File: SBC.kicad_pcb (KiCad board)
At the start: 4 copper layers, 0.6 x 0.9 mm, 128 parts, among them J1 MSD-1-A, J2 RJ45_Amphenol_RJMG1BD3B8K1ANR, J3 DX07S016JA1R1500, U1 MIC5501-3.0YM5, U10 USBLC6-2SC6, U11 USBLC6-2SC6, U12 USBLC6-2SC6, U2 TLV62569DBV, U3 TLV62569DBV, U4 TLV62569DBV, U5 Allwinner_V3s, U6 USBLC6-2SC6, U7 USBLC6-2SC6, U8 USBLC6-2SC6, U9 USBLC6-2SC6, Y1 Crystal

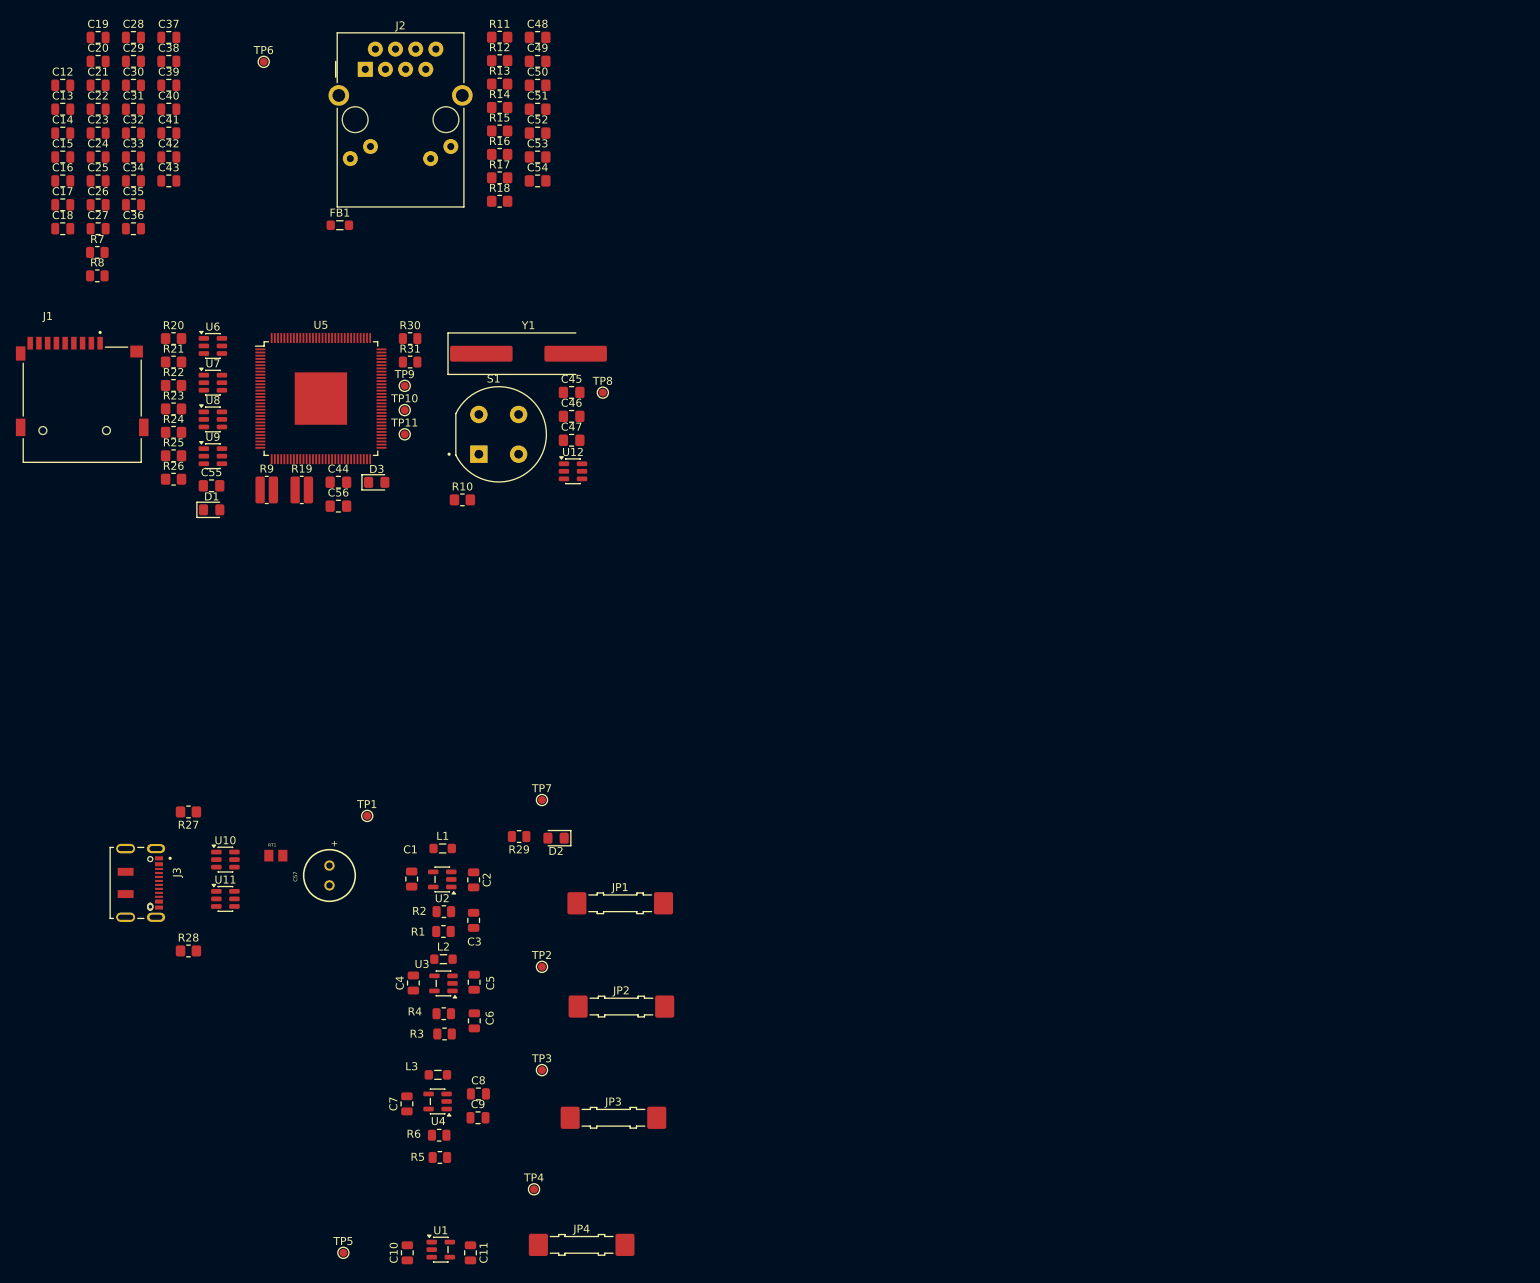
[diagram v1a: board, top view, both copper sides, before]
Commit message: arranged positions of all the components
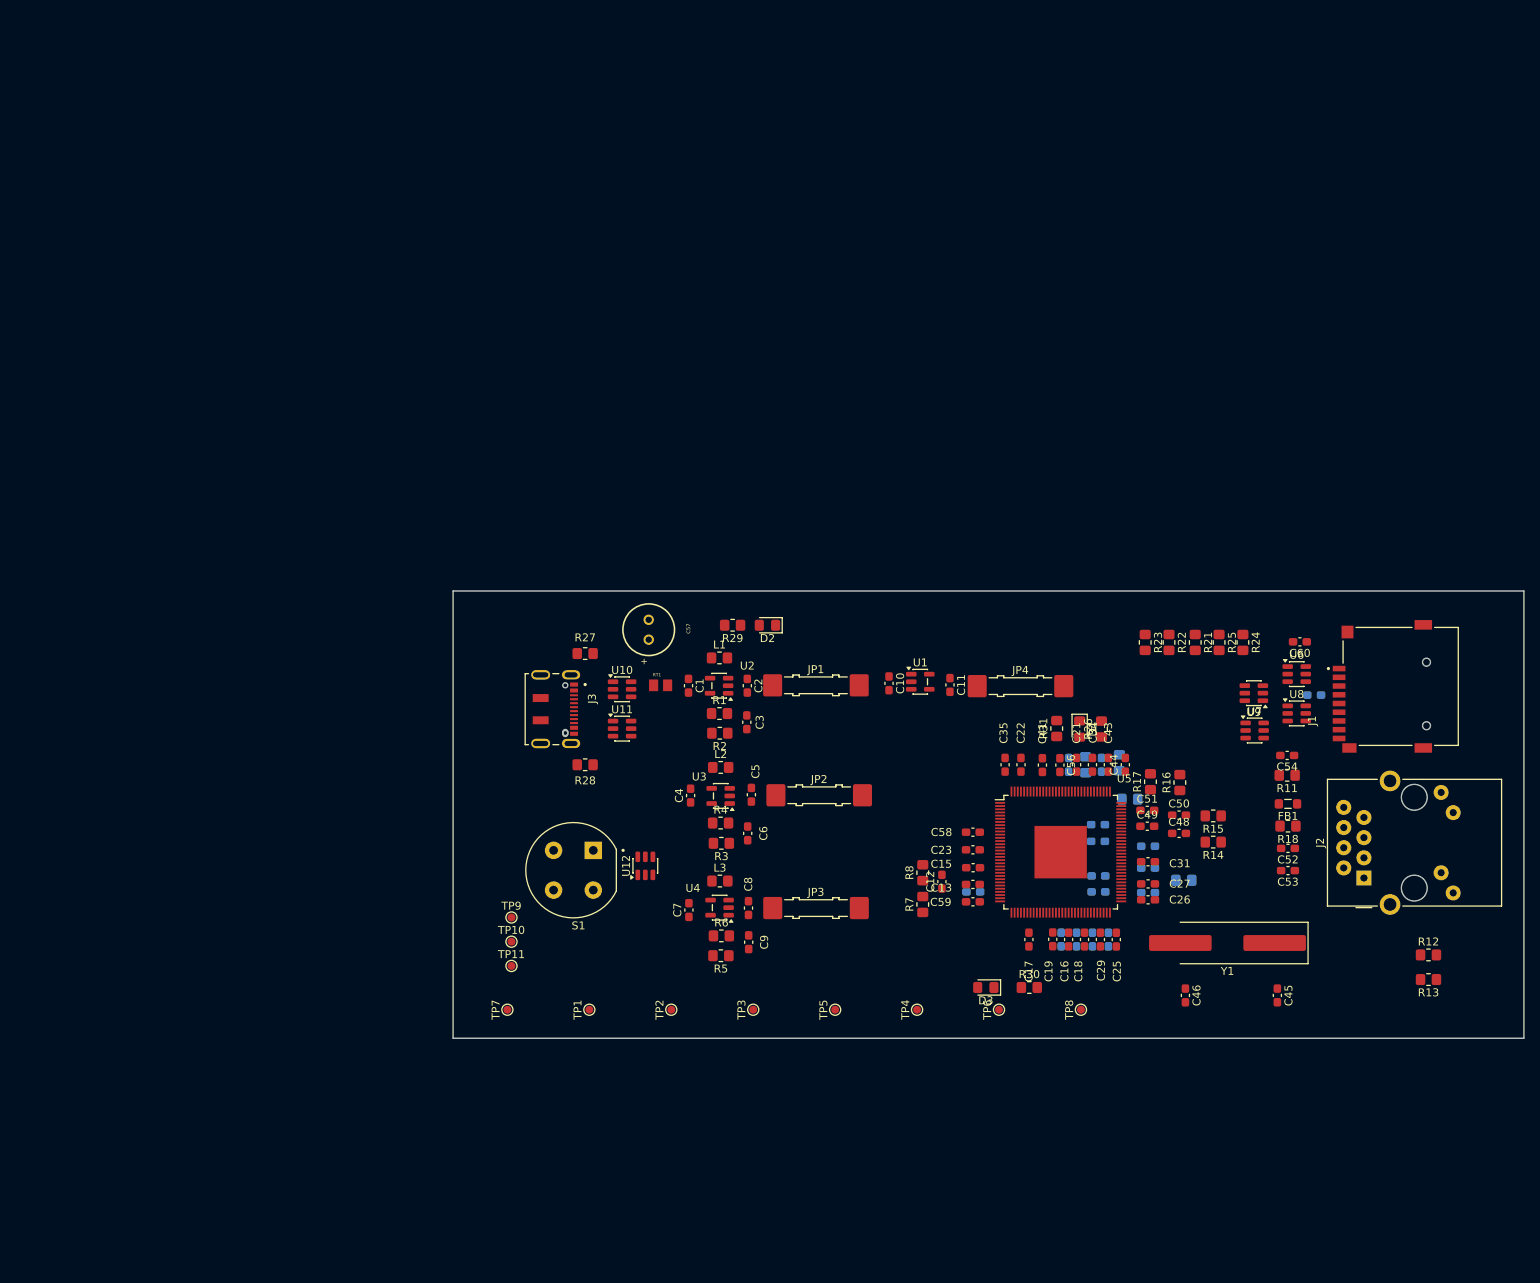
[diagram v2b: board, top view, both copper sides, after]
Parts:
- added C58: 100nF, Capacitor_SMD:C_0603_1608Metric_Pad1.08x0.95mm_HandSolder, F.Cu at (135.3, 116.1)
- added C59: 100nF, Capacitor_SMD:C_0603_1608Metric_Pad1.08x0.95mm_HandSolder, F.Cu at (135.3, 124.8)
- added C60: 22uF, Capacitor_SMD:C_0603_1608Metric_Pad1.08x0.95mm_HandSolder, F.Cu at (176.4, 92.1)
- C1, C10, C11, C12, C13, C15, C16, C17, C18, C19, C2, C21, C22, C23, C25, C26, C27, C29, C3, C31, C34, C35, C4, C41, C43, C5, C6, C7, C8, C9: footprint Capacitor_SMD:C_0805_2012Metric -> Capacitor_SMD:C_0603_1608Metric_Pad1.08x0.95mm_HandSolder
- C14, C20, C24, C28, C30, C32, C33, C36, C37, C38, C39, C40, C42: footprint Capacitor_SMD:C_0805_2012Metric -> Capacitor_SMD:C_0603_1608Metric_Pad1.08x0.95mm_HandSolder; moved to B.Cu
- C44, C45, C46, C48, C49, C50, C51, C52, C53, C54, C56: footprint Capacitor_SMD:C_0805_2012Metric_Pad1.18x1.45mm_HandSolder -> Capacitor_SMD:C_0603_1608Metric_Pad1.08x0.95mm_HandSolder
- C47, C55: footprint Capacitor_SMD:C_0805_2012Metric_Pad1.18x1.45mm_HandSolder -> Capacitor_SMD:C_0603_1608Metric_Pad1.08x0.95mm_HandSolder; moved to B.Cu
- L1, L2, L3: footprint Inductor_SMD:L_0805_2012Metric_Pad1.05x1.20mm_HandSolder -> Resistor_SMD:R_0805_2012Metric_Pad1.20x1.40mm_HandSolder
- R1, R2, R29, R3, R30, R31, R4, R5, R6, R7, R8: footprint Resistor_SMD:R_0805_2012Metric -> Resistor_SMD:R_0805_2012Metric_Pad1.20x1.40mm_HandSolder
- R10, R20: moved to B.Cu
- R19, R9: footprint Resistor_SMD:R_0612_1632Metric_Pad1.18x3.40mm_HandSolder -> Resistor_SMD:R_0805_2012Metric_Pad1.20x1.40mm_HandSolder; moved to B.Cu
- moved J1 169.7 mm to (189.1, 97.7), turned to 90 degrees
- moved C28 167.0 mm to (157.3, 123.7)
- moved C19 165.3 mm to (145.3, 129.5), turned to -90 degrees
- moved C20 165.0 mm to (157.3, 117.8)
- moved C29 164.4 mm to (151.3, 129.6), turned to -90 degrees
- moved C30 163.2 mm to (152.3, 129.6), turned to -90 degrees
- moved R13 162.4 mm to (192.6, 134.6), turned to 180 degrees
- moved R12 162.3 mm to (192.6, 131.5)
- moved J2 161.8 mm to (184.5, 121.8), turned to 90 degrees
- moved C14 161.6 mm to (146.4, 129.6), turned to -90 degrees
- moved C25 159.8 mm to (153.3, 129.6), turned to -90 degrees
- moved C31 159.0 mm to (157.3, 119.8)
- moved C16 158.6 mm to (147.3, 129.6), turned to -90 degrees
- moved C26 158.5 mm to (157.3, 124.6)
- moved C24 157.7 mm to (148.3, 129.6), turned to -90 degrees
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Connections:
- U6 pad 1: /Allwinner V3S/SDCO_CMD -> /Allwinner V3S/SDCO_D2
- U6 pad 3: /Allwinner V3S/SDCO_D0 -> /Allwinner V3S/SDCO_D3
- U6 pad 4: /Allwinner V3S/SDCO_D0 -> /Allwinner V3S/SDCO_D3
- U6 pad 6: /Allwinner V3S/SDCO_CMD -> /Allwinner V3S/SDCO_D2
- U7 pad 1: /Allwinner V3S/SDCO_D1 -> /Allwinner V3S/SDCO_D0
- U7 pad 3: /Allwinner V3S/SDCO_D2 -> /Allwinner V3S/SDCO_D1
- U7 pad 4: /Allwinner V3S/SDCO_D2 -> /Allwinner V3S/SDCO_D1
- U7 pad 6: /Allwinner V3S/SDCO_D1 -> /Allwinner V3S/SDCO_D0
- U8 pad 3: /Allwinner V3S/SDCO_D3 -> unconnected-(U8-I/O2-Pad3)
- U8 pad 4: /Allwinner V3S/SDCO_D3 -> unconnected-(U8-I/O2-Pad4)
- U9 pad 3: unconnected-(U9-I/O2-Pad3) -> /Allwinner V3S/SDCO_CMD
- U9 pad 4: unconnected-(U9-I/O2-Pad4) -> /Allwinner V3S/SDCO_CMD
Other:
- board size 0.6 x 0.9 mm -> 134.8 x 56.3 mm
